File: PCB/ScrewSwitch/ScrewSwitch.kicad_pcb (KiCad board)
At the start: 2 copper layers, 53.3 x 48.3 mm, 8 parts, among them J1 Screw_Terminal_Device_Output, J2 Screw_Terminal_Battery, J4 Conn_02x04_Odd_Even, SW1 SW_DIP_x01

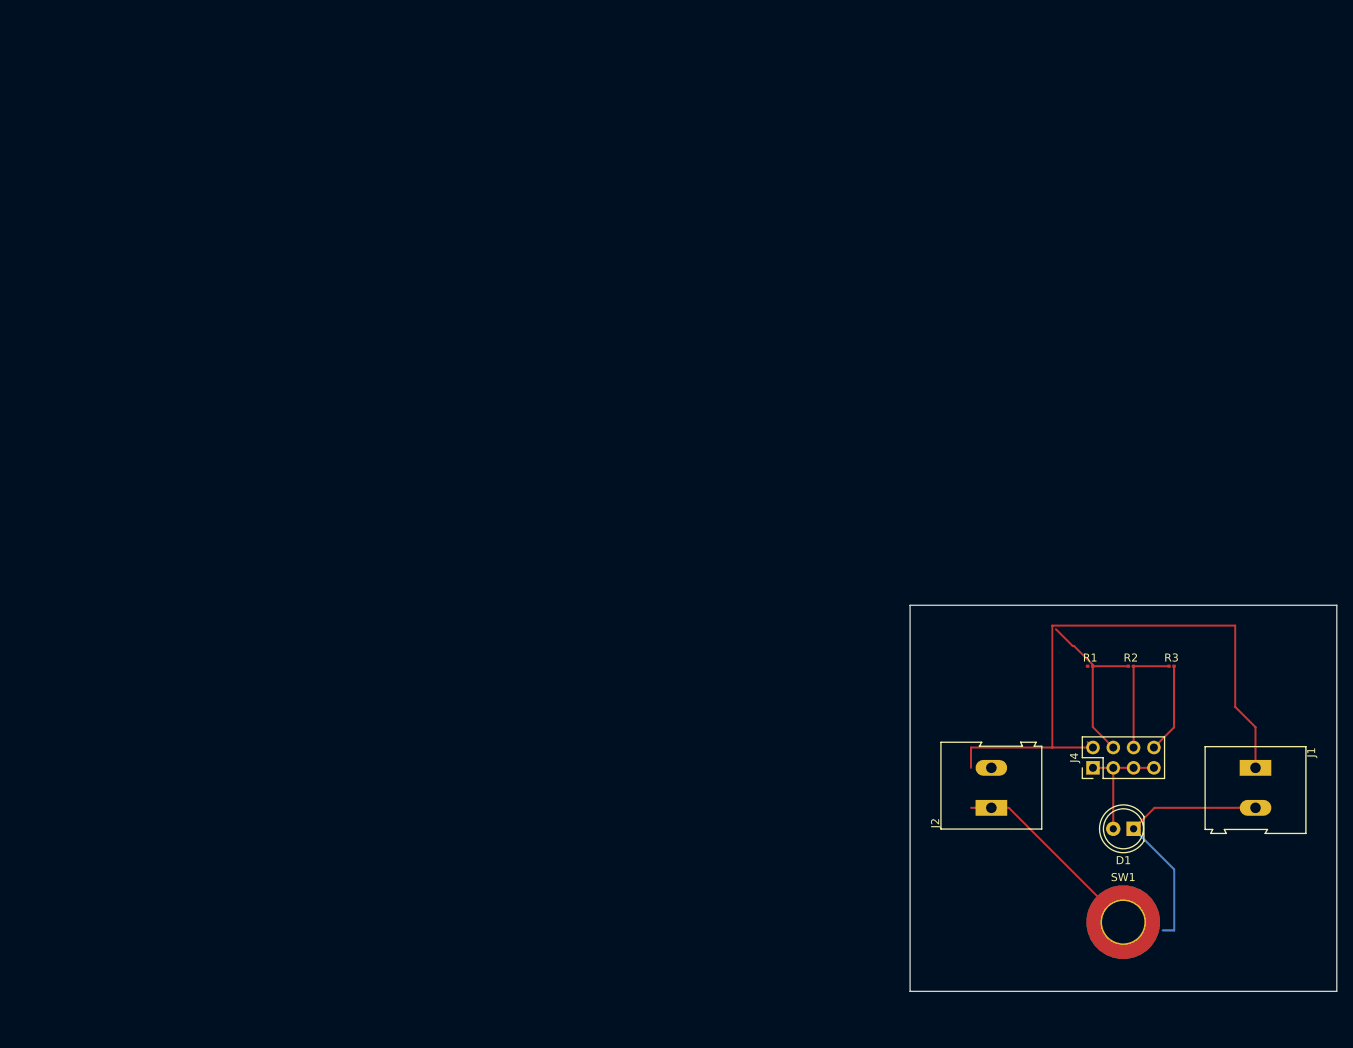
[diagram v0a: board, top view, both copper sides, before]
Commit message: Adds KiCad file updates for Screw Switch
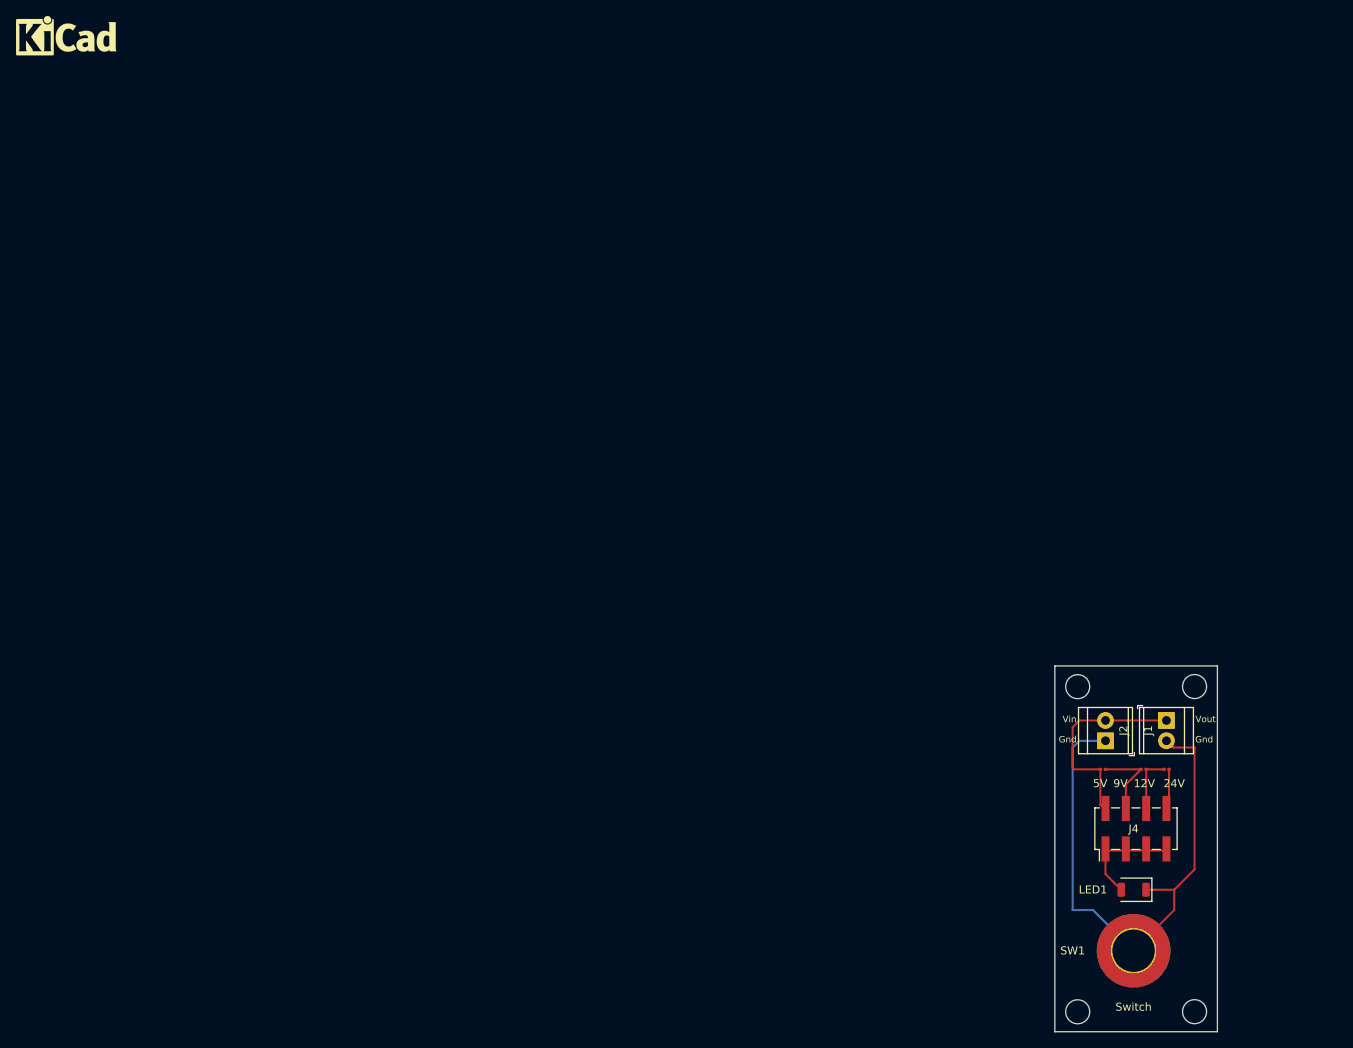
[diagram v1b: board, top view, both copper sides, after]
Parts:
- added BT1: Battery, Symbol:KiCad-Logo_5mm_SilkScreen, F.Cu at (6.28, 2.98)
- added H1: MountingHole, MountingHole:MountingHole_3mm, F.Cu at (132.7, 83.8)
- added H2: MountingHole, MountingHole:MountingHole_3mm, F.Cu at (147.3, 83.8)
- added H3: MountingHole, MountingHole:MountingHole_3mm, F.Cu at (132.7, 124.5)
- added H4: MountingHole, MountingHole:MountingHole_3mm, F.Cu at (147.3, 124.5)
- J1, J2: footprint TerminalBlock:TerminalBlock_Altech_AK300-2_P5.00mm -> TerminalBlock_TE-Connectivity:TerminalBlock_TE_282834-2_1x02_P2.54mm_Horizontal
- J4: footprint Connector_PinHeader_2.54mm:PinHeader_2x04_P2.54mm_Vertical -> Connector_PinHeader_2.54mm:PinHeader_2x04_P2.54mm_Vertical_SMD
- LED1: renamed from D1; footprint LED_THT:LED_D5.0mm -> LED_SMD:LED_1206_3216Metric_ReverseMount_Hole1.8x2.4mm
- R3: value 600 -> 560
- moved J2 16.5 mm to (136.2, 90.6)
- moved R2 13.0 mm to (140.9, 94.2)
- moved R1 13.0 mm to (135.9, 94.2)
- moved R3 12.9 mm to (143.8, 94.2)
- moved J1 12.6 mm to (143.8, 88.1)
- moved J4 9.31 mm to (140.0, 101.6)
- moved LED1 7.62 mm to (139.7, 109.2)
- moved SW1 3.80 mm to (139.7, 116.8)
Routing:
- net Net-(BT1-+): track 75.7 -> 26.3 mm
- net Net-(BT1--): track 24.9 -> 70.4 mm
- net Net-(J1-Pin_2): track 32.6 -> 0.00 mm
- net Net-(J4-Pin_4): track 22.3 -> 10.3 mm
- net Net-(J4-Pin_6): track 14.7 -> 7.30 mm
- net Net-(J4-Pin_8): track 11.2 -> 5.21 mm
- net Net-(J4-Pin_1): track 15.2 -> 13.3 mm
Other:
- board size 53.3 x 48.3 mm -> 20.3 x 45.7 mm
- board text added: "12V"
- board text added: "24V"
- board text added: "5V"
- board text added: "9V"
- board text added: "Designed By Peter Pak"
- board text added: "GLHF"
- board text added: "Gnd"
- board text added: "On"
- board text added: "ScrewSwitch V1.0"
- board text added: "Switch"
- board text added: "Vin"
- board text added: "Vout"

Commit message: Adds updated kicad files.
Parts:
- R1, R2, R3: footprint Resistor_SMD:R_0201_0603Metric -> Resistor_SMD:R_0402_1005Metric
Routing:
- net Net-(J4-Pin_4): track 10.3 -> 9.66 mm
